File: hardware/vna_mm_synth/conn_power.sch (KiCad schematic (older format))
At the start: 32 parts, among them U301 CONN_SMA_2GND, U302 CONN_SMA_2GND

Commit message: added power supply sequencing
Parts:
- U202: renamed from U?; symbol 74xx:74HC244 -> vna_mm_synth-rescue:74HC244-74xx
- gave numbers to parts that had none: 10
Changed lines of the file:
@@
 	7200 7150 7200 7250
 $Comp
-L power:GND #PWR?
+L power:GND #PWR0105
 U 1 1 5D8BFB3D
 P 8550 3850
-AR Path="/5AB8DC0D/5D8BFB3D" Ref="#PWR?"  Part="1"
+AR Path="/5AB8DC0D/5D8BFB3D" Ref="#PWR0105"  Part="1"
 AR Path="/5D4AD94E/5D8BFB3D" Ref="#PWR?"  Part="1"
-F 0 "#PWR?" H 8550 3600 50  0001 C CNN
+F 0 "#PWR0105" H 8550 3600 50  0001 C CNN
 F 1 "GND" H 8550 3700 50  0000 C CNN
 F 2 "" H 8550 3850 50  0001 C CNN
@@
 	8550 3750 8550 3850
 $Comp
-L power:+5VP #PWR?
+L power:+5VP #PWR0129
 U 1 1 5D8BFB44
 P 8550 1750
-F 0 "#PWR?" H 8550 1600 50  0001 C CNN
+F 0 "#PWR0129" H 8550 1600 50  0001 C CNN
 F 1 "+5VP" H 8565 1923 50  0000 C CNN
 F 2 "" H 8550 1750 50  0001 C CNN
@@
 $EndComp
 $Comp
-L Device:C_Small C?
+L Device:C_Small C231
 U 1 1 5D8BFB4A
 P 8800 2450
-F 0 "C?" H 8892 2496 50  0000 L CNN
+F 0 "C231" H 8892 2496 50  0000 L CNN
 F 1 "100 nF" H 8892 2405 50  0000 L CNN
 F 2 "" H 8800 2450 50  0001 C CNN
@@
 $EndComp
 $Comp
-L power:GND #PWR?
+L power:GND #PWR0130
 U 1 1 5D8BFB50
 P 8800 2600
-F 0 "#PWR?" H 8800 2350 50  0001 C CNN
+F 0 "#PWR0130" H 8800 2350 50  0001 C CNN
 F 1 "GND" H 8805 2427 50  0000 C CNN
 F 2 "" H 8800 2600 50  0001 C CNN
@@
 	8550 2200 8550 2750
 $Comp
-L Device:L_Small L?
+L Device:L_Small L203
 U 1 1 5D8BFB5A
 P 8550 2000
-F 0 "L?" H 8598 2046 50  0000 L CNN
+F 0 "L203" H 8598 2046 50  0000 L CNN
 F 1 "L_Small" H 8598 1955 50  0000 L CNN
 F 2 "" H 8550 2000 50  0001 C CNN
@@
 Connection ~ 8550 2200
 $Comp
-L vna_mm:LM71CIMF U?
+L vna_mm:LM71CIMF U203
 U 1 1 5D8BFB63
 P 8550 3250
-F 0 "U?" H 8728 3296 50  0000 L CNN
+F 0 "U203" H 8728 3296 50  0000 L CNN
 F 1 "LM71CIMF" H 8728 3205 50  0000 L CNN
 F 2 "TO_SOT_Packages_SMD:SOT-23-5" H 7700 3800 50  0001 C CNN
@@
 $EndComp
 $Comp
-L Device:R_Small R?
+L Device:R_Small R218
 U 1 1 5D8BFB69
 P 6800 3050
-F 0 "R?" V 6700 2900 50  0000 C CNN
+F 0 "R218" V 6700 2900 50  0000 C CNN
 F 1 "22" V 6700 3050 50  0000 C CNN
 F 2 "" H 6800 3050 50  0001 C CNN
@@
 $EndComp
 $Comp
-L Device:R_Small R?
+L Device:R_Small R219
 U 1 1 5D8BFB6F
 P 6800 3250
-F 0 "R?" V 6700 3100 50  0000 C CNN
+F 0 "R219" V 6700 3100 50  0000 C CNN
 F 1 "22" V 6700 3250 50  0000 C CNN
 F 2 "" H 6800 3250 50  0001 C CNN
@@
 $EndComp
 $Comp
-L Device:C_Small C?
+L Device:C_Small C229
 U 1 1 5D8BFB75
 P 7450 3700
-F 0 "C?" H 7542 3746 50  0000 L CNN
+F 0 "C229" H 7542 3746 50  0000 L CNN
 F 1 "100 pF" H 7542 3655 50  0000 L CNN
 F 2 "" H 7450 3700 50  0001 C CNN
@@
 $EndComp
 $Comp
-L Device:C_Small C?
+L Device:C_Small C230
 U 1 1 5D8BFB7B
 P 7900 3700
-F 0 "C?" H 7992 3746 50  0000 L CNN
+F 0 "C230" H 7992 3746 50  0000 L CNN
 F 1 "100 pF" H 7992 3655 50  0000 L CNN
 F 2 "" H 7900 3700 50  0001 C CNN
@@
 $EndComp
 $Comp
-L Device:C_Small C?
+L Device:C_Small C228
 U 1 1 5D8BFB81
 P 7000 3700
-F 0 "C?" H 7092 3746 50  0000 L CNN
+F 0 "C228" H 7092 3746 50  0000 L CNN
 F 1 "100 pF" H 7092 3655 50  0000 L CNN
 F 2 "" H 7000 3700 50  0001 C CNN
@@
 $EndComp
 $Comp
-L Device:R_Small R?
+L Device:R_Small R220
 U 1 1 5D8BFB87
 P 6800 3450
-F 0 "R?" V 6700 3300 50  0000 C CNN
+F 0 "R220" V 6700 3300 50  0000 C CNN
 F 1 "22" V 6700 3450 50  0000 C CNN
 F 2 "" H 6800 3450 50  0001 C CNN
@@
 	8050 3450 7900 3450
 $Comp
-L power:GND #PWR?
+L power:GND #PWR0131
 U 1 1 5D8BFB90
 P 7900 3850
-AR Path="/5AB8DC0D/5D8BFB90" Ref="#PWR?"  Part="1"
+AR Path="/5AB8DC0D/5D8BFB90" Ref="#PWR0131"  Part="1"
 AR Path="/5D4AD94E/5D8BFB90" Ref="#PWR?"  Part="1"
-F 0 "#PWR?" H 7900 3600 50  0001 C CNN
+F 0 "#PWR0131" H 7900 3600 50  0001 C CNN
 F 1 "GND" H 7900 3700 50  0000 C CNN
 F 2 "" H 7900 3850 50  0001 C CNN
@@
 $EndComp
 $Comp
-L power:GND #PWR?
+L power:GND #PWR0132
 U 1 1 5D8BFB96
 P 7450 3850
-AR Path="/5AB8DC0D/5D8BFB96" Ref="#PWR?"  Part="1"
+AR Path="/5AB8DC0D/5D8BFB96" Ref="#PWR0132"  Part="1"
 AR Path="/5D4AD94E/5D8BFB96" Ref="#PWR?"  Part="1"
-F 0 "#PWR?" H 7450 3600 50  0001 C CNN
+F 0 "#PWR0132" H 7450 3600 50  0001 C CNN
 F 1 "GND" H 7450 3700 50  0000 C CNN
 F 2 "" H 7450 3850 50  0001 C CNN
@@
 $EndComp
 $Comp
-L power:GND #PWR?
+L power:GND #PWR0133
 U 1 1 5D8BFB9C
 P 7000 3850
-AR Path="/5AB8DC0D/5D8BFB9C" Ref="#PWR?"  Part="1"
+AR Path="/5AB8DC0D/5D8BFB9C" Ref="#PWR0133"  Part="1"
 AR Path="/5D4AD94E/5D8BFB9C" Ref="#PWR?"  Part="1"
-F 0 "#PWR?" H 7000 3600 50  0001 C CNN
+F 0 "#PWR0133" H 7000 3600 50  0001 C CNN
 F 1 "GND" H 7000 3700 50  0000 C CNN
 F 2 "" H 7000 3850 50  0001 C CNN
@@
 STUSB4500 for USB PD sink?
 $Comp
-L Connector_Generic:Conn_02x10_Odd_Even J?
+L Connector_Generic:Conn_02x10_Odd_Even J201
 U 1 1 5D643699
 P 4100 6150
-F 0 "J?" H 4150 6767 50  0000 C CNN
+F 0 "J201" H 4150 6767 50  0000 C CNN
 F 1 "Conn_02x10_Odd_Even" H 4150 6676 50  0000 C CNN
 F 2 "" H 4100 6150 50  0001 C CNN
@@
 $EndComp
 $Comp
-L 74xx:74HC244 U?
+L vna_mm_synth-rescue:74HC244-74xx U?
 U 1 1 5D645FB5
 P 7750 6650
-F 0 "U?" H 7350 7600 50  0000 C CNN
+AR Path="/5D645FB5" Ref="U?"  Part="1"
+AR Path="/5AB8DC0D/5D645FB5" Ref="U202"  Part="1"
+F 0 "U202" H 7350 7600 50  0000 C CNN
 F 1 "74HC244" H 7450 7500 50  0000 C CNN
 F 2 "" H 7750 6650 50  0001 C CNN

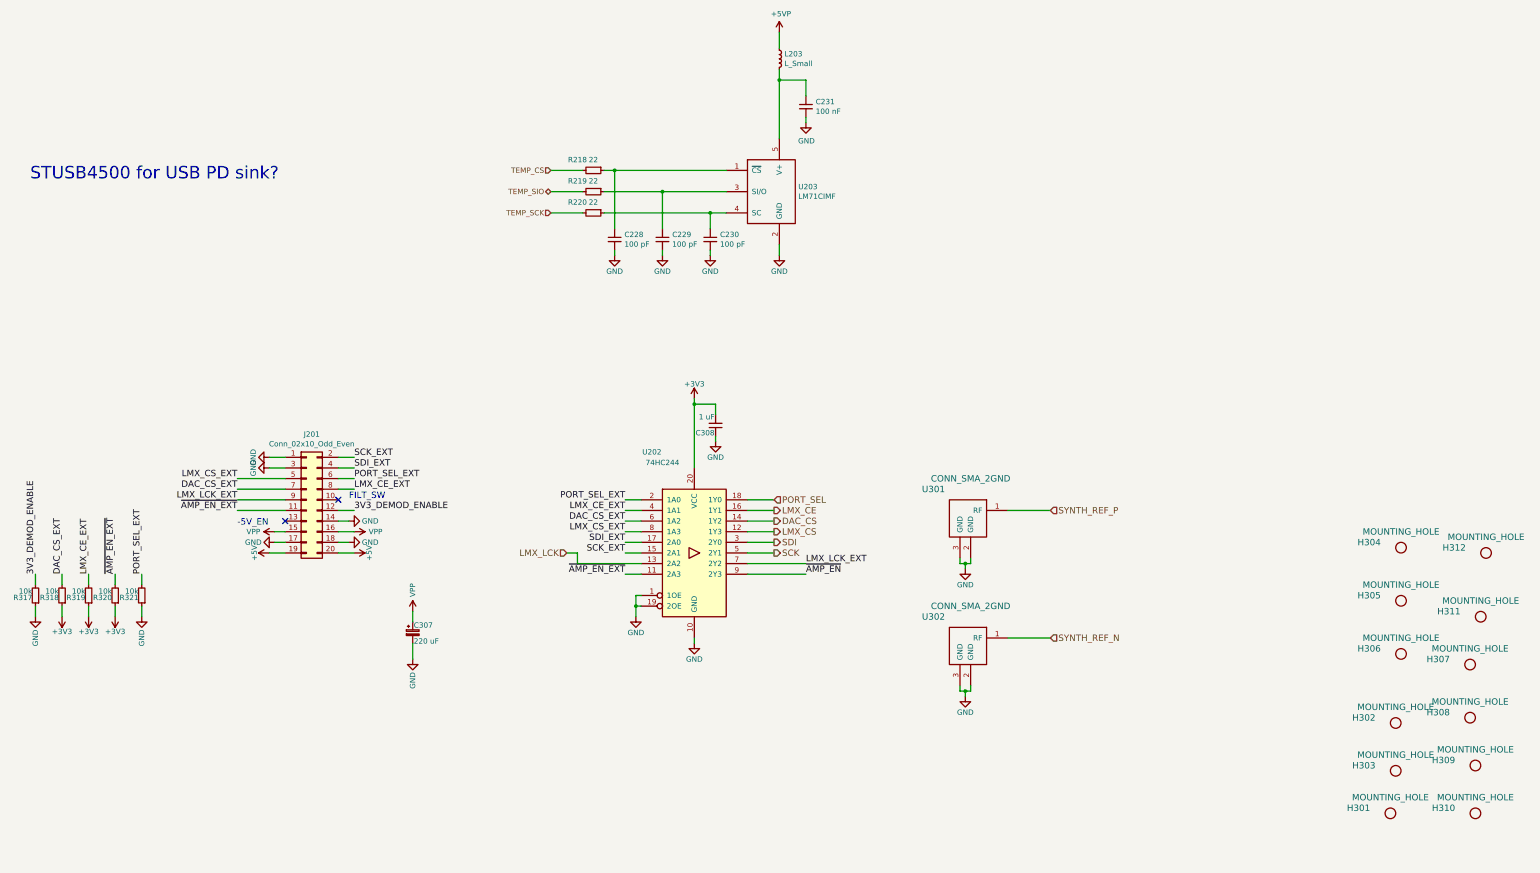
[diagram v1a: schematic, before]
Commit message: added trl cal and set of breakout boards
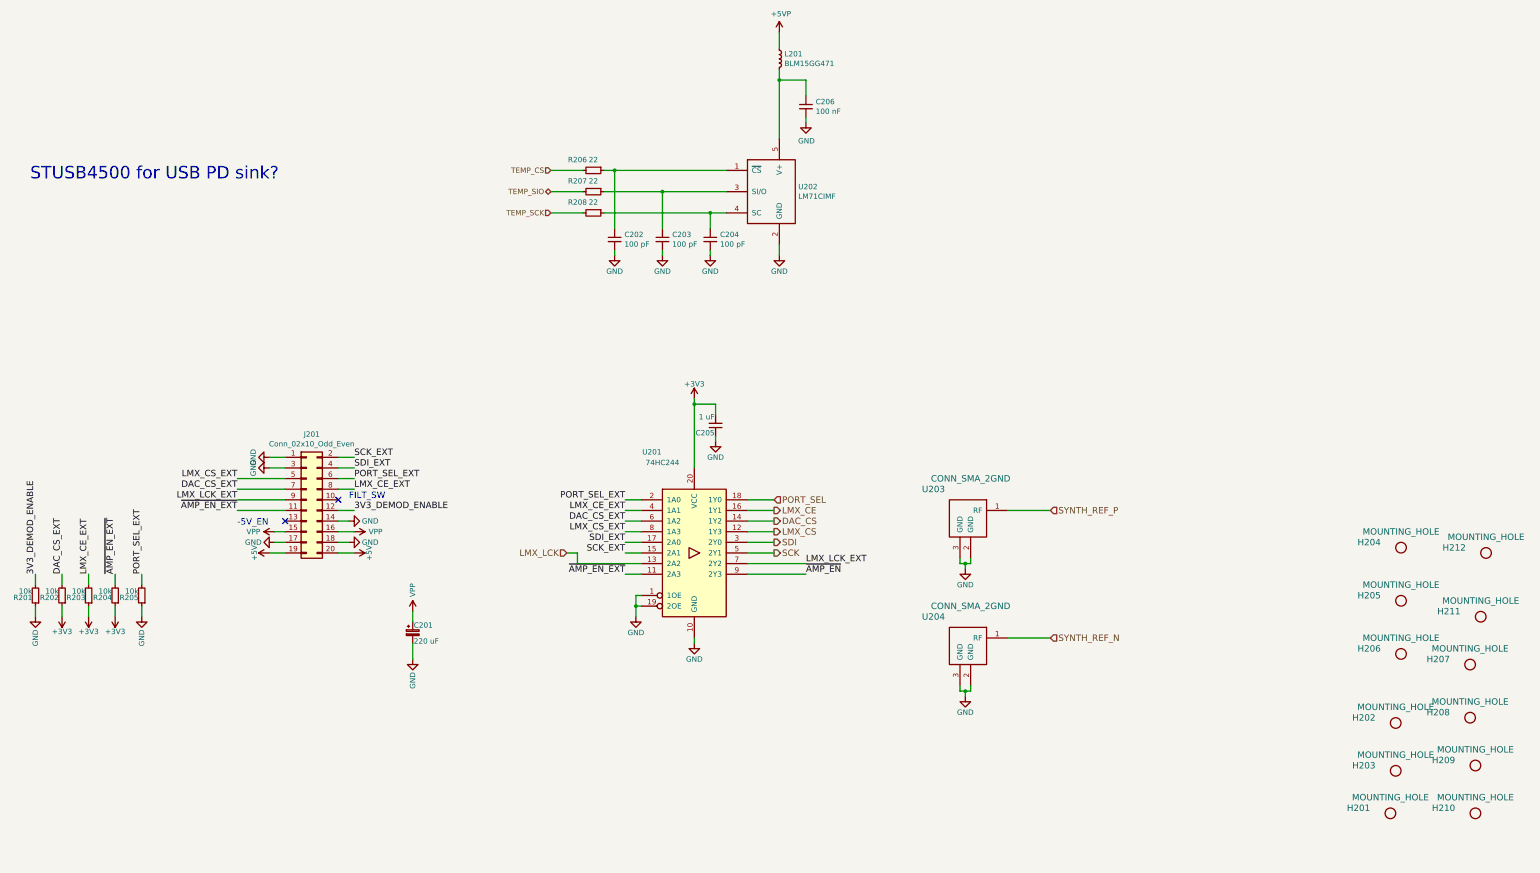
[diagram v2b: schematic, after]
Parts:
- C202: renamed from C228; footprint (none) -> Capacitors_SMD:C_0402
- C203: renamed from C229; footprint (none) -> Capacitors_SMD:C_0402
- C204: renamed from C230; footprint (none) -> Capacitors_SMD:C_0402
- C206: renamed from C231; footprint (none) -> Capacitors_SMD:C_0402
- L201: renamed from L203; value L_Small -> BLM15GG471
- R206: renamed from R218; footprint (none) -> Resistors_SMD:R_0402
- R207: renamed from R219; footprint (none) -> Resistors_SMD:R_0402
- R208: renamed from R220; footprint (none) -> Resistors_SMD:R_0402
- renumbered C307 to C201, C308 to C205, H301 to H201, H302 to H202, H303 to H203, H304 to H204, H305 to H205, H306 to H206, H307 to H207, H308 to H208, H309 to H209, H310 to H210, H311 to H211, H312 to H212, R317 to R201, R318 to R202, R319 to R203, R320 to R204, R321 to R205, U202 to U201, U203 to U202, U301 to U203, U302 to U204

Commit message: fixed mirrored 3.3V regulator on sequencer board, created and assigned footprints for synth
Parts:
- L201: footprint (none) -> Resistors_SMD:R_0402
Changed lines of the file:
@@
 F 0 "L201" H 8598 2046 50  0000 L CNN
 F 1 "BLM15GG471" H 8598 1955 50  0000 L CNN
-F 2 "" H 8550 2000 50  0001 C CNN
+F 2 "Resistors_SMD:R_0402" H 8550 2000 50  0001 C CNN
 F 3 "~" H 8550 2000 50  0001 C CNN
 	1    8550 2000

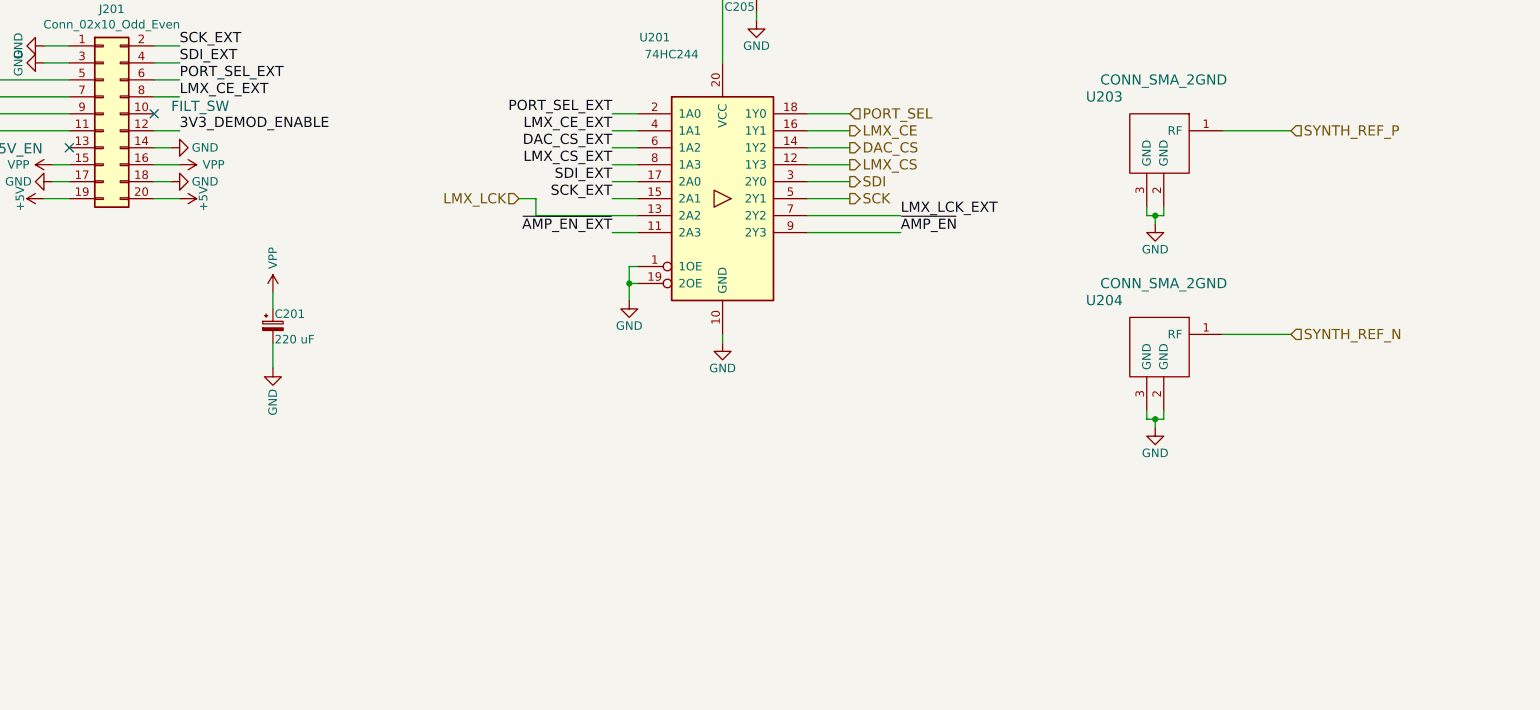
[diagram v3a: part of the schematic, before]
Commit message: started variable filter bias circuitry - added 15V bias
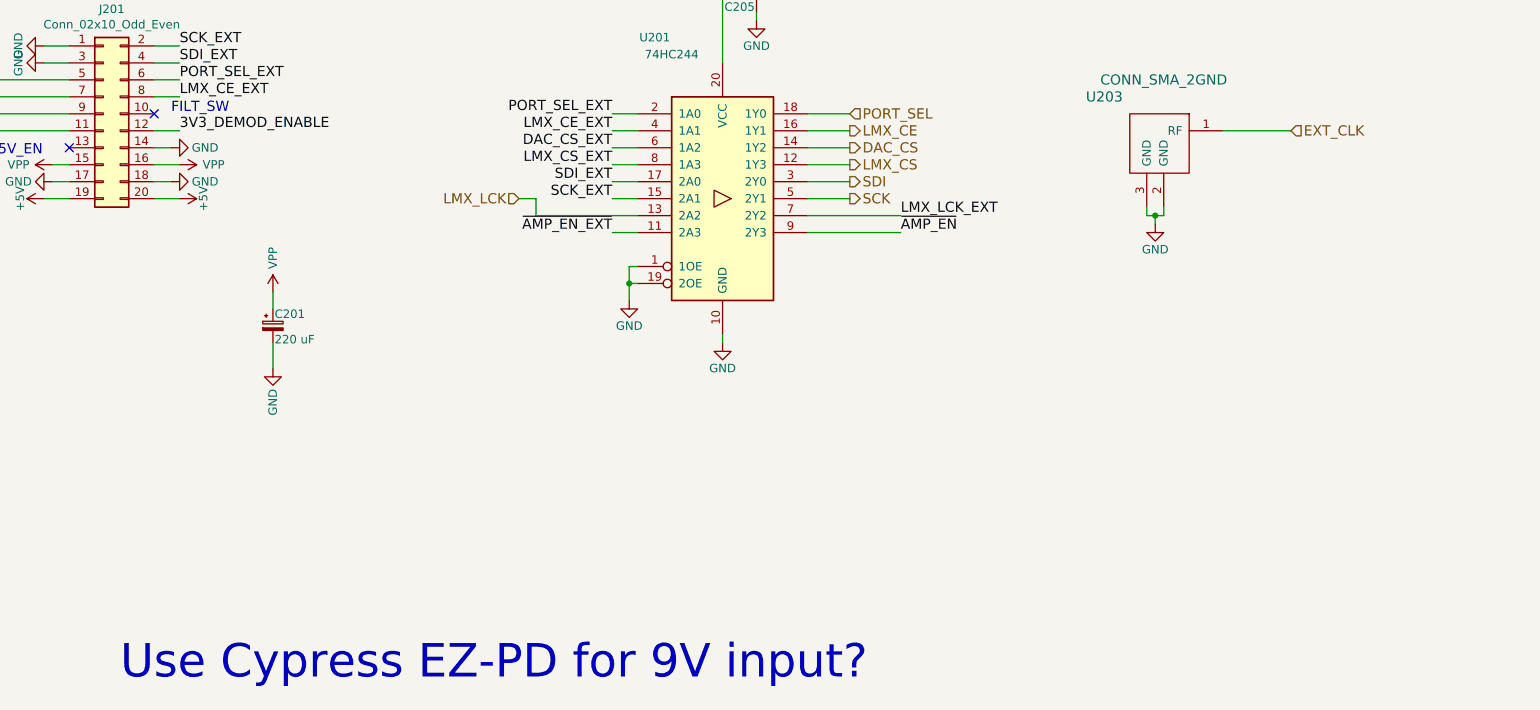
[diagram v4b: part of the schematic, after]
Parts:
- removed U204: CONN_SMA_2GND, vna_footprints:734120110_ufl_umc, symbol conn_sma_2gnd:CONN_SMA_2GND
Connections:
- net SYNTH_REF_P renamed EXT_CLK
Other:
- note added: "Use Cypress EZ-PD for 9V input?"
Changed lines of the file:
@@
 $Descr A3 16535 11693
 encoding utf-8
-Sheet 2 11
+Sheet 2 12
 Title ""
 Date ""
@@
 $EndComp
 Text HLabel 11100 6250 2    60   Input ~ 0
-SYNTH_REF_P
-$Comp
-L conn_sma_2gnd:CONN_SMA_2GND U204
-U 1 1 5AB949C1
-P 10300 7450
-F 0 "U204" H 10000 7650 60  0000 C CNN
-F 1 "CONN_SMA_2GND" H 10350 7750 60  0000 C CNN
-F 2 "vna_footprints:734120110_ufl_umc" H 10300 7450 60  0001 C CNN
-F 3 "" H 10300 7450 60  0000 C CNN
-	1    10300 7450
-	1    0    0    -1
-$EndComp
-$Comp
-L power:GND #PWR0228
-U 1 1 5AB949C7
-P 10300 8000
-F 0 "#PWR0228" H 10300 7750 50  0001 C CNN
-F 1 "GND" H 10300 7850 50  0000 C CNN
-F 2 "" H 10300 8000 50  0001 C CNN
-F 3 "" H 10300 8000 50  0001 C CNN
-	1    10300 8000
-	1    0    0    -1
-$EndComp
-Text HLabel 11100 7450 2    60   Input ~ 0
-SYNTH_REF_N
+EXT_CLK
 Text Label 4550 6250 0    60   ~ 0
 3V3_DEMOD_ENABLE
@@
 	11100 6250 10700 6250
 Wire Wire Line
-	10250 7900 10250 7950
-Wire Wire Line
-	10250 7950 10300 7950
-Wire Wire Line
-	10350 7950 10350 7900
-Wire Wire Line
-	10300 7950 10300 8000
-Connection ~ 10300 7950
-Wire Wire Line
-	11100 7450 10700 7450
-Wire Wire Line
 	8250 6150 8500 6150
 Wire Wire Line
@@
 Wire Wire Line
 	10300 6750 10350 6750
-Wire Wire Line
-	10300 7950 10350 7950
 Wire Wire Line
 	7750 5250 7750 5850
@@
 Wire Wire Line
 	7750 7450 7750 7500
+Text Notes 4200 9500 0    197  ~ 0
+Use Cypress EZ-PD for 9V input?
 $EndSCHEMATC

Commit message: cleanup and update vna mm synth schematic for modern kicad libraries
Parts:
- removed H201, H202, H203, H204, H205, H206, H207, H208, H209, H210, H211, H212: MOUNTING_HOLE, Mounting_Holes:MountingHole_2-5mm, symbol mounting_hole:MOUNTING_HOLE
- removed U201: 74HC244, symbol vna_mm_synth-rescue:74HC244-74xx
- removed U203: CONN_SMA_2GND, vna_footprints:734120110_ufl_umc, symbol conn_sma_2gnd:CONN_SMA_2GND
- added J?: Conn_Coaxial, symbol Connector:Conn_Coaxial
- added U?: 74HC244, symbol 74xx:74HC244
- C201: footprint Capacitors_SMD:c_elec_6.3x5.8 -> Capacitor_SMD:CP_Elec_6.3x5.8; symbol device:CP_Small -> Device:CP_Small
- C202, C203, C204, C206: footprint Capacitors_SMD:C_0402 -> Capacitor_SMD:C_0402_1005Metric
- C205: footprint Capacitors_SMD:C_0402 -> Capacitor_SMD:C_0402_1005Metric; symbol device:C_Small -> Device:C_Small
- L201: footprint Resistors_SMD:R_0402 -> Inductor_SMD:L_0402_1005Metric
- R201, R202, R203, R204, R205: footprint Resistors_SMD:R_0402 -> Resistor_SMD:R_0402_1005Metric; symbol device:R_Small -> Device:R_Small
- R206, R207, R208: footprint Resistors_SMD:R_0402 -> Resistor_SMD:R_0402_1005Metric
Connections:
- net +3V3: now also U?.20 (VCC)
- net DAC_CS: now also U?.14 (1Y2)
- net DAC_CS_EXT: now also U?.6 (1A2)
- net EXT_CLK: now also J?.1 (In)
- net GND: now also J?.2 (Ext), U?.1 (1OE), U?.10 (GND), U?.19 (2OE)
- net LMX_CE: now also U?.16 (1Y1)
- net LMX_CE_EXT: now also U?.4 (1A1)
- net LMX_CS: now also U?.12 (1Y3)
- net LMX_CS_EXT: now also U?.8 (1A3)
- net LMX_LCK: now also U?.13 (2A2)
- net LMX_LCK_EXT: now also U?.7 (2Y2)
- net PORT_SEL: now also U?.18 (1Y0)
- net PORT_SEL_EXT: now also U?.2 (1A0)
- net SCK: now also U?.5 (2Y1)
- net SCK_EXT: now also U?.15 (2A1)
- net SDI: now also U?.3 (2Y0)
- net SDI_EXT: now also U?.17 (2A0)
- net ~AMP_EN: now also U?.9 (2Y3)
- net ~AMP_EN_EXT: now also U?.11 (2A3)

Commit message: footprint assignment
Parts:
- J202: renamed from J?; footprint (none) -> Connector_Coaxial:SMA_Amphenol_132289_EdgeMount
- gave numbers to parts that had none: 1
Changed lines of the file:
@@
 Use Cypress EZ-PD for 9V input?
 $Comp
-L 74xx:74HC244 U?
+L 74xx:74HC244 U201
 U 1 1 5DF0D107
 P 7750 6650
-F 0 "U?" H 7750 7631 50  0000 C CNN
+F 0 "U201" H 7750 7631 50  0000 C CNN
 F 1 "74HC244" H 7750 7540 50  0000 C CNN
 F 2 "" H 7750 6650 50  0001 C CNN
@@
 $EndComp
 $Comp
-L Connector:Conn_Coaxial J?
+L Connector:Conn_Coaxial J202
 U 1 1 5DF110B4
 P 10500 6250
-F 0 "J?" H 10428 6488 50  0000 C CNN
+F 0 "J202" H 10428 6488 50  0000 C CNN
 F 1 "Conn_Coaxial" H 10428 6397 50  0000 C CNN
-F 2 "" H 10500 6250 50  0001 C CNN
+F 2 "Connector_Coaxial:SMA_Amphenol_132289_EdgeMount" H 10500 6250 50  0001 C CNN
 F 3 " ~" H 10500 6250 50  0001 C CNN
 	1    10500 6250
